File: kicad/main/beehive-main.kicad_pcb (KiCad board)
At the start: 2 copper layers, 0 parts

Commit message: feat: place the main board
72 x 56 mm with the Feather on the left and its antenna end past the bottom edge. Battery, solar and the hive RJ45 sit on the top edge, CELL1-2 on the right and CELL3-4 on the bottom; the charger, protection and monitors run in a column beside the Feather and the NAU7802 faces its terminals.
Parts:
- added C1: 10u 25V, Capacitor_SMD:C_0603_1608Metric, F.Cu at (136.0, 126.5)
- added C10: 100n, Capacitor_SMD:C_0603_1608Metric, F.Cu at (155.5, 133.5)
- added C11: 330p, Capacitor_SMD:C_0603_1608Metric, F.Cu at (157.8, 129.2)
- added C12: 100n, Capacitor_SMD:C_0603_1608Metric, F.Cu at (139.5, 123.8)
- added C13: 100n, Capacitor_SMD:C_0603_1608Metric, F.Cu at (130.5, 128.3)
- added C14: 10u, Capacitor_SMD:C_0603_1608Metric, F.Cu at (147.5, 120.0)
- added C2: 10u, Capacitor_SMD:C_0603_1608Metric, F.Cu at (143.0, 126.5)
- added C3: 100n, Capacitor_SMD:C_0603_1608Metric, F.Cu at (127.3, 110.0)
- added C4: 470u, Capacitor_SMD:CP_Elec_6.3x7.7, F.Cu at (131.0, 133.5)
- added C5: 1u, Capacitor_SMD:C_0603_1608Metric, F.Cu at (145.0, 135.4)
- added C6: 1u, Capacitor_SMD:C_0603_1608Metric, F.Cu at (145.0, 128.6)
- added C8: 100n, Capacitor_SMD:C_0603_1608Metric, F.Cu at (155.5, 129.0)
- added C9: 100n, Capacitor_SMD:C_0603_1608Metric, F.Cu at (145.0, 132.0)
- added H1: MountingHole, MountingHole:MountingHole_3.2mm_M3, F.Cu at (103.5, 103.5)
- added H2: MountingHole, MountingHole:MountingHole_3.2mm_M3, F.Cu at (148.0, 103.5)
- added H3: MountingHole, MountingHole:MountingHole_3.2mm_M3, F.Cu at (131.0, 152.5)
- added H4: MountingHole, MountingHole:MountingHole_3.2mm_M3, F.Cu at (168.5, 152.5)
- added J1: RJHSE5380, Connector_RJ:RJ45_Amphenol_RJHSE5380, F.Cu at (158.3, 108.2)
- added J2: FEATHER_L, Connector_PinSocket_2.54mm:PinSocket_1x16_P2.54mm_Vertical, F.Cu at (104.0, 114.0)
- added J3: FEATHER_R, Connector_PinSocket_2.54mm:PinSocket_1x12_P2.54mm_Vertical, F.Cu at (124.3, 152.1)
- added J4: SOLAR, Connector_Phoenix_MC:PhoenixContact_MC_1,5_2-G-3.5_1x02_P3.50mm_Horizontal, F.Cu at (140.0, 108.5)
- added J5: BATTERY (1 -, 2 +), Connector_JST:JST_PH_B2B-PH-K_1x02_P2.00mm_Vertical, F.Cu at (129.0, 104.0)
- added J6: CELL1, Connector_Phoenix_MC:PhoenixContact_MC_1,5_3-G-3.5_1x03_P3.50mm_Horizontal, F.Cu at (163.5, 127.0)
- added J7: CELL2, Connector_Phoenix_MC:PhoenixContact_MC_1,5_3-G-3.5_1x03_P3.50mm_Horizontal, F.Cu at (163.5, 140.1)
- added J8: CELL3, Connector_Phoenix_MC:PhoenixContact_MC_1,5_3-G-3.5_1x03_P3.50mm_Horizontal, F.Cu at (141.9, 147.5)
- added J9: CELL4, Connector_Phoenix_MC:PhoenixContact_MC_1,5_3-G-3.5_1x03_P3.50mm_Horizontal, F.Cu at (155.0, 147.5)
- added Q1: AO3401A, Package_TO_SOT_SMD:SOT-23, F.Cu at (140.0, 113.5)
- added Q2: FS8205A, Package_TO_SOT_SMD:SOT-23-6, F.Cu at (130.0, 117.7)
- added R1: 0.1, Resistor_SMD:R_1206_3216Metric, F.Cu at (140.0, 117.0)
- added R10: 33, Resistor_SMD:R_0603_1608Metric, F.Cu at (119.5, 141.9)
- added R11: 33, Resistor_SMD:R_0603_1608Metric, F.Cu at (119.5, 139.4)
- added R12: 10k, Resistor_SMD:R_0603_1608Metric, F.Cu at (139.5, 132.0)
- added R13: 10k, Resistor_SMD:R_0603_1608Metric, F.Cu at (136.6, 130.0)
- added R2: 820, Resistor_SMD:R_0603_1608Metric, F.Cu at (143.0, 130.0)
- added R3: 100, Resistor_SMD:R_0603_1608Metric, F.Cu at (130.0, 110.0)
- added R4: 1k, Resistor_SMD:R_0603_1608Metric, F.Cu at (133.3, 113.4)
- added R5: 0.1, Resistor_SMD:R_1206_3216Metric, F.Cu at (130.0, 121.5)
- added R6: 47, Resistor_SMD:R_0603_1608Metric, F.Cu at (158.8, 135.0)
- added R7: 47, Resistor_SMD:R_0603_1608Metric, F.Cu at (158.8, 132.0)
- added R8: 3.3k, Resistor_SMD:R_0603_1608Metric, F.Cu at (119.5, 147.5)
- added R9: 3.3k, Resistor_SMD:R_0603_1608Metric, F.Cu at (119.5, 150.0)
- added TP1: BAT+, TestPoint:TestPoint_Pad_D1.5mm, F.Cu at (128.0, 139.0)
- added TP10: WS, TestPoint:TestPoint_Pad_D1.5mm, F.Cu at (130.5, 144.1)
- added TP11: SCK, TestPoint:TestPoint_Pad_D1.5mm, F.Cu at (133.1, 144.1)
- added TP12: SD, TestPoint:TestPoint_Pad_D1.5mm, F.Cu at (135.6, 144.1)
- added TP13: CHG, TestPoint:TestPoint_Pad_D1.5mm, F.Cu at (128.0, 146.6)
- added TP14: PG, TestPoint:TestPoint_Pad_D1.5mm, F.Cu at (130.5, 146.6)
- added TP15: DRDY, TestPoint:TestPoint_Pad_D1.5mm, F.Cu at (133.1, 146.6)
- added TP16: AVDD, TestPoint:TestPoint_Pad_D1.5mm, F.Cu at (135.6, 146.6)
- added TP2: BAT-, TestPoint:TestPoint_Pad_D1.5mm, F.Cu at (130.5, 139.0)
- added TP3: VBAT_F, TestPoint:TestPoint_Pad_D1.5mm, F.Cu at (133.1, 139.0)
- added TP4: SOLAR, TestPoint:TestPoint_Pad_D1.5mm, F.Cu at (135.6, 139.0)
- added TP5: CHG_IN, TestPoint:TestPoint_Pad_D1.5mm, F.Cu at (128.0, 141.5)
- added TP6: GND, TestPoint:TestPoint_Pad_D1.5mm, F.Cu at (130.5, 141.5)
- added TP7: +3V3, TestPoint:TestPoint_Pad_D1.5mm, F.Cu at (133.1, 141.5)
- added TP8: SDA, TestPoint:TestPoint_Pad_D1.5mm, F.Cu at (135.6, 141.5)
- added TP9: SCL, TestPoint:TestPoint_Pad_D1.5mm, F.Cu at (128.0, 144.1)
- added U1: INA226 (0x40), Package_SO:MSOP-10_3x3mm_P0.5mm, F.Cu at (139.5, 120.5)
- added U2: BQ24210, Package_SON:WSON-10-1EP_2x3mm_P0.5mm_EP0.84x2.4mm, F.Cu at (139.5, 128.0)
- added U3: DW01A, Package_TO_SOT_SMD:SOT-23-6, F.Cu at (130.0, 113.5)
- added U4: INA226 (0x41), Package_SO:MSOP-10_3x3mm_P0.5mm, F.Cu at (130.5, 125.0)
- added U5: NAU7802, Package_SO:SOIC-16_3.9x9.9mm_P1.27mm, F.Cu at (150.0, 131.0)
- added U6: SRV05-4, Package_TO_SOT_SMD:SOT-23-6, F.Cu at (152.5, 120.5)
- added U7: SRV05-4, Package_TO_SOT_SMD:SOT-23-6, F.Cu at (157.5, 120.5)
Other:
- board outline added: 72 x 56 mm

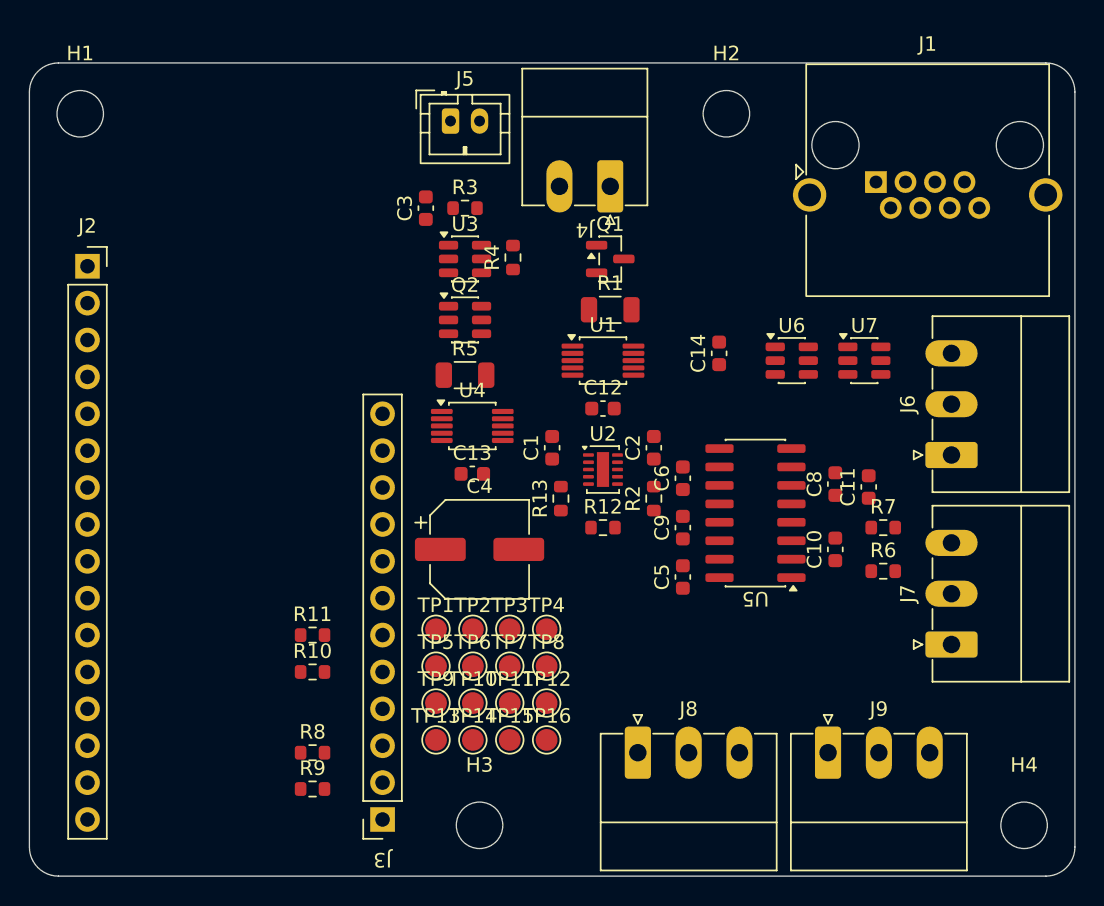
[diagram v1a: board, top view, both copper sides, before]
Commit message: feat: route the main board
Freerouting with bottom-layer traces costed 6x, so signals stay on top and the bottom is free for a ground plane: 1480 mm of top copper against 187 mm on the bottom, 61 vias. Power nets are 0.3 mm with 0.15 mm clearance to reach the INA226's 0.5 mm pins, and the minimum track is JLCPCB's 0.1 mm for neck-downs between through-hole pins.
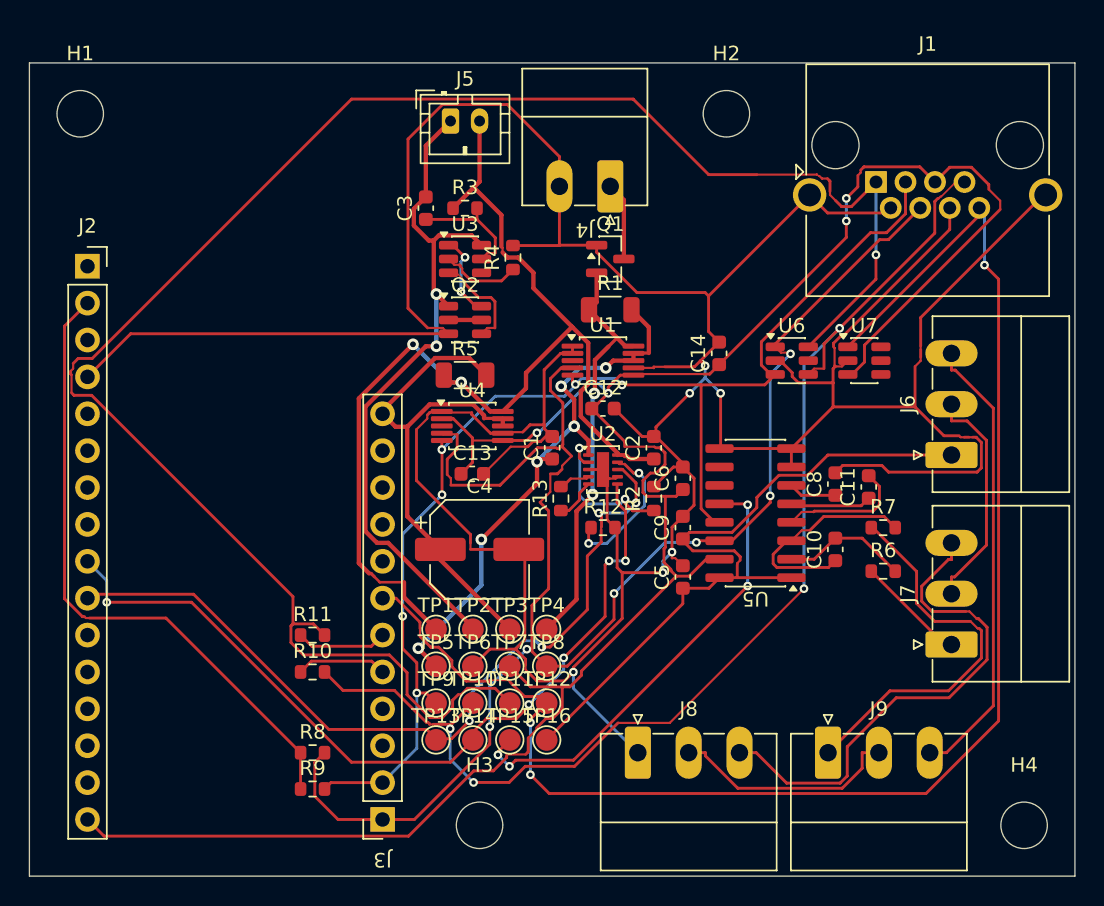
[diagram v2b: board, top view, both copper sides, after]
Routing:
- net /GND: track 0.00 -> 289.2 mm, vias 0 -> 6
- net /+3V3: track 0.00 -> 149.6 mm, vias 0 -> 4
- net /SCK: track 0.00 -> 129.0 mm, vias 0 -> 1
- net /SDA: track 0.00 -> 111.8 mm, vias 0 -> 6
- net /SD: track 0.00 -> 104.6 mm, vias 0 -> 3
- net /SCL: track 0.00 -> 86.9 mm, vias 0 -> 6
- net /WS: track 0.00 -> 82.8 mm, vias 0 -> 4
- net /BAT+: track 0.00 -> 74.5 mm, vias 0 -> 2
- net /PG: track 0.00 -> 57.9 mm, vias 0 -> 5
- net /CHG: track 0.00 -> 56.8 mm, vias 0 -> 4
- net /AVDD: track 0.00 -> 49.5 mm
- net /BAT-: track 0.00 -> 47.8 mm, vias 0 -> 2
- net /3V3_AON: track 0.00 -> 44.2 mm
- net /CHG_IN: track 0.00 -> 38.9 mm, vias 0 -> 6
- net /VBAT_F: track 0.00 -> 36.5 mm
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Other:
- outline, holes or cut-outs redrawn

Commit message: feat: pour ground on both layers of the main board
Both pours stop short of the strip under the Feather's antenna end, and the board corners are rounded again after routing.
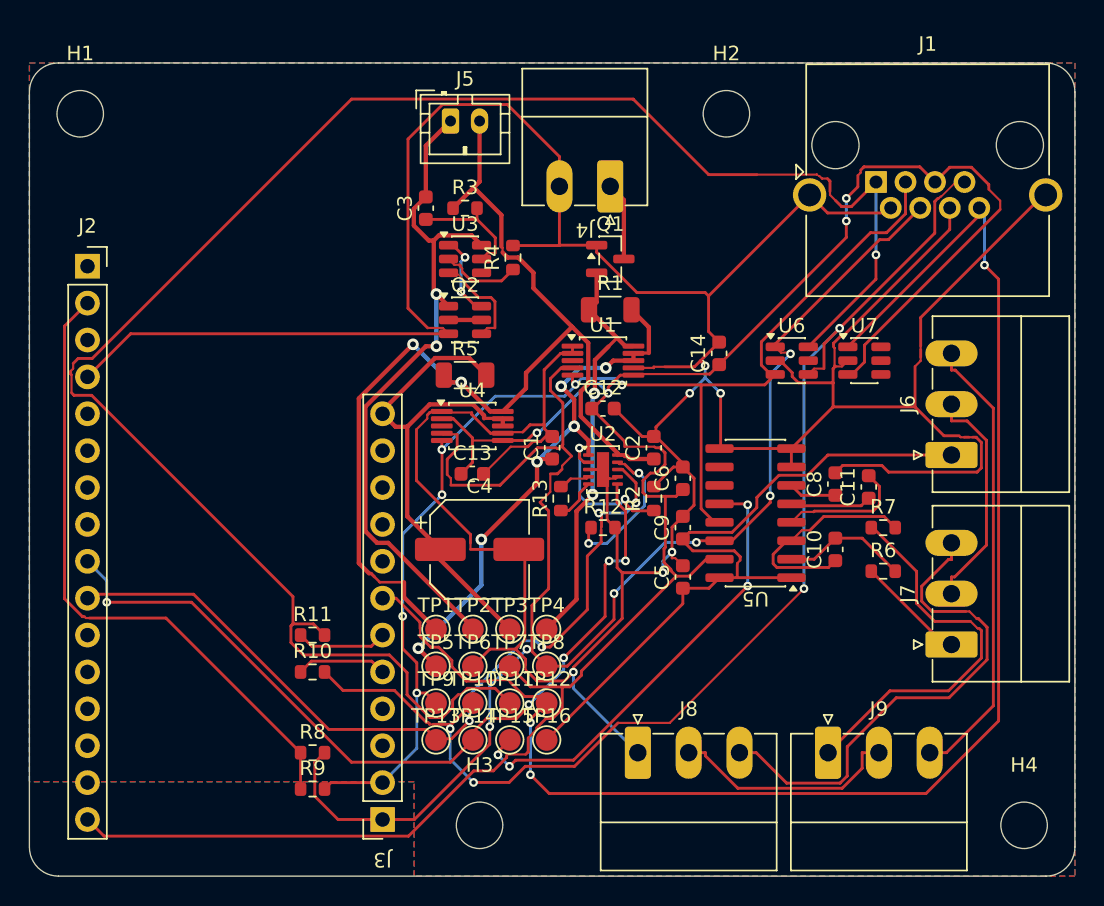
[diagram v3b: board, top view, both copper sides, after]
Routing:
- added copper zone on B.Cu, net /GND
- added copper zone on F.Cu, net /GND
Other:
- outline, holes or cut-outs redrawn
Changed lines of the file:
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@@
 		)
 	)
+	(gr_arc
+		(start 100 102)
+		(mid 100.585786 100.585786)
+		(end 102 100)
+		(stroke
+			(width 0.05)
+			(type default)
+		)
+		(layer "Edge.Cuts")
+	)
 	(gr_line
-		(start 100 100)
-		(end 172 100)
+		(start 100 154)
+		(end 100 102)
 		(stroke
 			(width 0.05)
@@
 	)
 	(gr_line
-		(start 100 156)
-		(end 100 100)
+		(start 102 100)
+		(end 170 100)
+		(stroke
+			(width 0.05)
+			(type default)
+		)
+		(layer "Edge.Cuts")
+	)
+	(gr_arc
+		(start 102 156)
+		(mid 100.585786 155.414213)
+		(end 100 154)
+		(stroke
+			(width 0.05)
+			(type default)
+		)
+		(layer "Edge.Cuts")
+	)
+	(gr_arc
+		(start 170 100)
+		(mid 171.414213 100.585786)
+		(end 172 102)
 		(stroke
 			(width 0.05)
@@
 	)
 	(gr_line
-		(start 172 100)
-		(end 172 156)
+		(start 170 156)
+		(end 102 156)
 		(stroke
 			(width 0.05)
@@
 	)
 	(gr_line
-		(start 172 156)
-		(end 100 156)
+		(start 172 102)
+		(end 172 154)
+		(stroke
+			(width 0.05)
+			(type default)
+		)
+		(layer "Edge.Cuts")
+	)
+	(gr_arc
+		(start 172 154)
+		(mid 171.414213 155.414213)
+		(end 170 156)
 		(stroke
 			(width 0.05)
@@
 		(net "/PROT_D")
 	)
+	(zone
+		(net "/GND")
+		(layer "F.Cu")
+		(name "GND top")
+		(hatch edge 0.508)
+		(connect_pads
+			(clearance 0.2)
+		)
+		(min_thickness 0.2)
+		(fill yes
+			(thermal_gap 0.5)
+			(thermal_bridge_width 0.5)
+			(island_removal_mode 0)
+		)
+		(polygon
+			(pts
+				(xy 100 100) (xy 172 100) (xy 172 156) (xy 126.5 156) (xy 126.5 149.5) (xy 100 149.5)
+			)
+		)
+	)
+	(zone
+		(net "/GND")
+		(layer "B.Cu")
+		(name "GND bottom")
+		(hatch edge 0.508)
+		(connect_pads
+			(clearance 0.2)
+		)
+		(min_thickness 0.2)
+		(fill yes
+			(thermal_gap 0.5)
+			(thermal_bridge_width 0.5)
+			(island_removal_mode 0)
+		)
+		(polygon
+			(pts
+				(xy 100 100) (xy 172 100) (xy 172 156) (xy 126.5 156) (xy 126.5 149.5) (xy 100 149.5)
+			)
+		)
+	)
 	(embedded_fonts no)
